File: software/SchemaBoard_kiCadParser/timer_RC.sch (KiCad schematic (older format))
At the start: 13 parts, among them SW11 button, U1 LM555 Timer

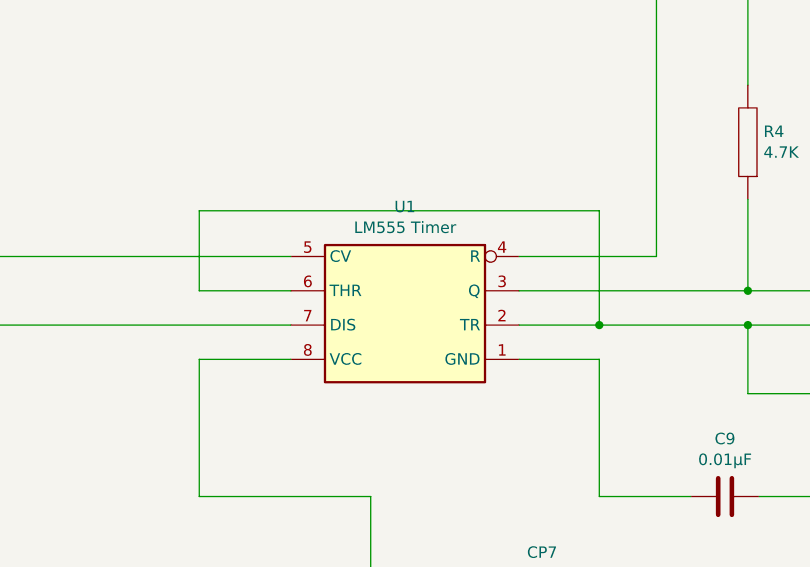
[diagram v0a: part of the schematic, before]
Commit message: change tutorial to guide mode
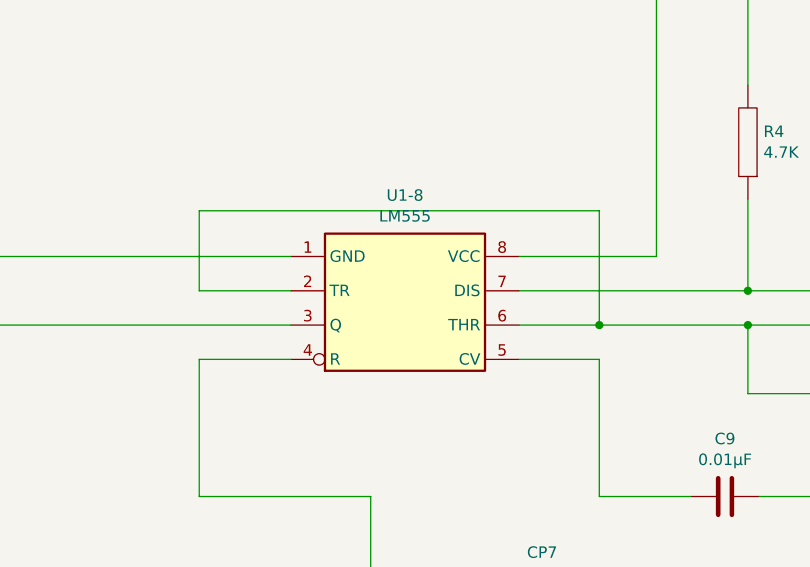
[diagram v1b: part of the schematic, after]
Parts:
- removed U1: LM555 Timer, symbol schemaboard:LM555
- added U1-8: LM555, symbol schemaboard:LM555
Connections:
- net GND: now also U1-8.1 (GND)
- net at C9.2: now also U1-8.5 (CV)
- net at C10.2, R5.1: now also U1-8.2 (TR), U1-8.6 (THR)
- net at R4.1, R5.2: now also U1-8.7 (DIS)
- net at CP7.1, R4.2, SW11.2 (D): now also U1-8.8 (VCC)
- net at CP6.1: now also U1-8.3 (Q)
- net at CP7.2, R2.1: now also U1-8.4 (R)
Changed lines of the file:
@@
 $EndDescr
-$Comp
-L schemaboard:LM555 U1
-U 1 1 5D4D75EC
-P 4050 4000
-F 0 "U1" H 4050 3533 50  0000 C CNN
-F 1 "LM555 Timer" H 4050 3624 50  0000 C CNN
-F 2 "" H 4050 4000 50  0001 C CNN
-F 3 "http://www.ti.com/lit/ds/symlink/lm555.pdf" H 4050 4000 50  0001 C CNN
-	1    4050 4000
-	-1   0    0    1
-$EndComp
 $Comp
 L schemaboard:Resistor R2
@@
 Wire Wire Line
 	6850 6100 6850 6900
+$Comp
+L schemaboard:LM555 U1-8
+U 1 1 5D7B2B89
+P 4050 3950
+F 0 "U1-8" H 4050 4417 50  0000 C CNN
+F 1 "LM555" H 4050 4326 50  0000 C CNN
+F 2 "" H 4050 3950 50  0001 C CNN
+F 3 "http://www.ti.com/lit/ds/symlink/lm555.pdf" H 4050 3950 50  0001 C CNN
+	1    4050 3950
+	1    0    0    -1
+$EndComp
 $EndSCHEMATC
